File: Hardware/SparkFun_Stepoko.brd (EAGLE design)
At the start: 150 x 80 mm, 175 parts, among them J1 AVR ISP, Q1 16MHZ, Q2 100A/100V, U1 ATMEGA328, U2 CY7C65213, U3 74LVC1G04, U4 LM25011, U5 DRV8811, U6 74HC7014D, U7 74AHC1G08, U8 DRV8811, U9 DRV8811

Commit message: made changes from design review
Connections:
- net GND: now also U6.13
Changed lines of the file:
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@@
 <?xml version="1.0" encoding="utf-8"?>
 <!DOCTYPE eagle SYSTEM "eagle.dtd">
-<eagle version="6.5.0">
+<eagle version="6.6.0">
 <drawing>
 <settings>
@@
 <via x="58.3" y="39.9" extent="1-16" drill="0.508" diameter="0.254"/>
 <via x="56.9" y="39.9" extent="1-16" drill="0.508" diameter="0.254"/>
+<contactref element="U6" pad="13"/>
 </signal>
 <signal name="N$28">

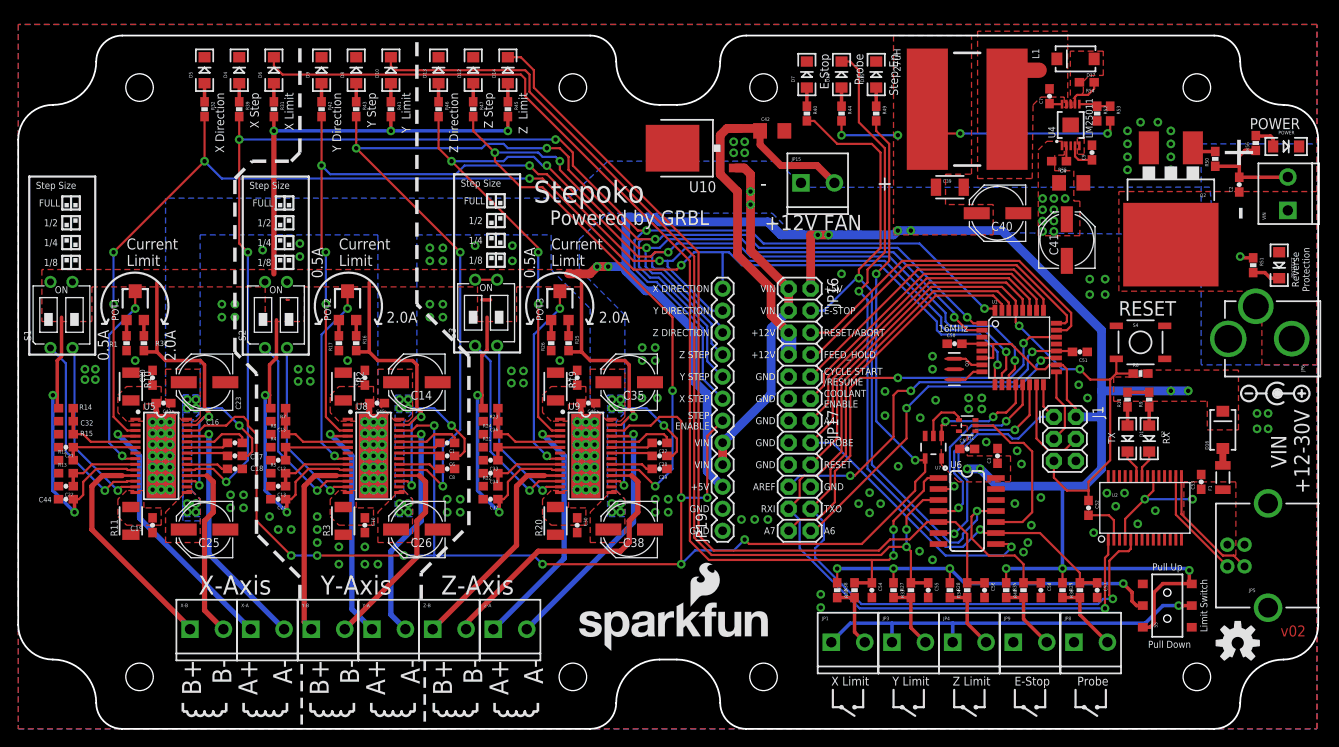
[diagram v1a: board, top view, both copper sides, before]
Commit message: fixed all issued in github
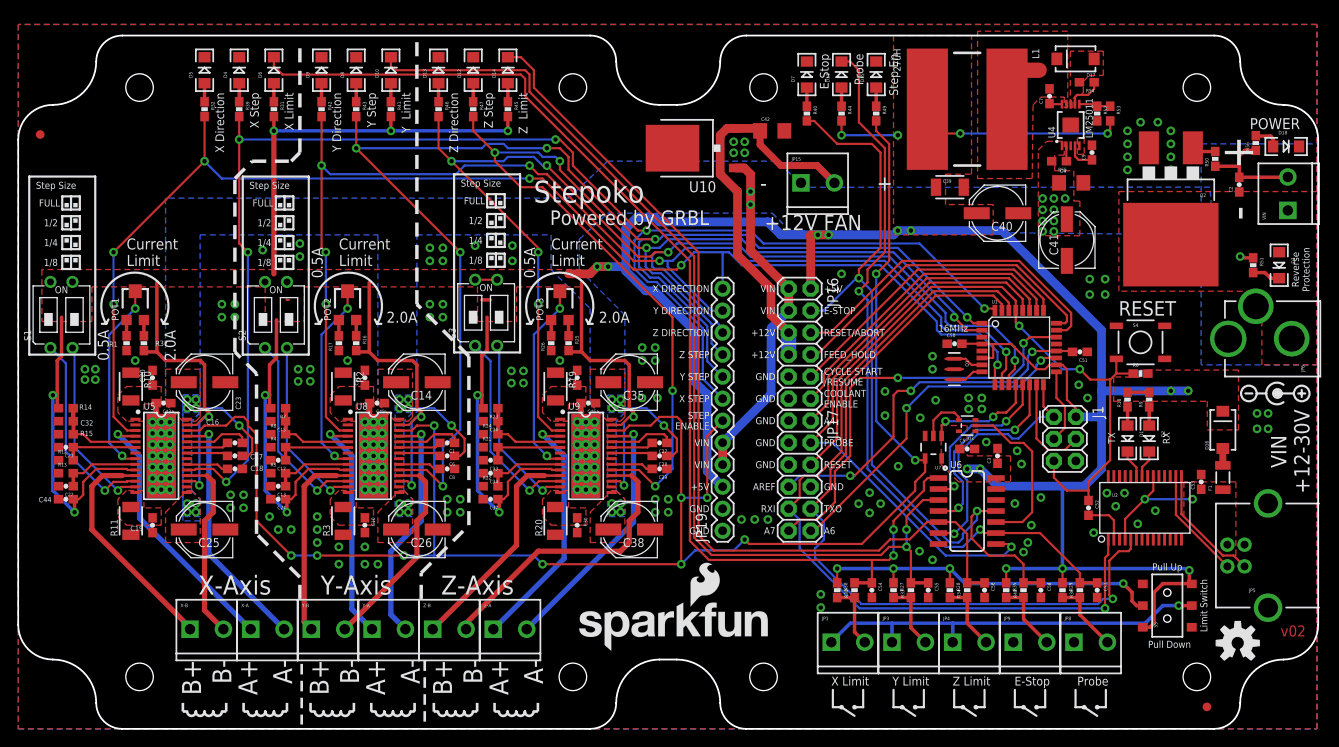
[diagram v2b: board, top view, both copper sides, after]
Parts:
- added FID1, FID2: FIDUCIAL1X2, SparkFun-Aesthetics:FIDUCIAL-1X2
- renumbered POWER to D18, PROTECT to D3
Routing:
- net 5V: track 532.5 -> 531.8 mm
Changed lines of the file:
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@@
 <?xml version="1.0" encoding="utf-8"?>
 <!DOCTYPE eagle SYSTEM "eagle.dtd">
-<eagle version="6.6.0">
+<eagle version="6.5.0">
 <drawing>
 <settings>
@@
 <setting verticaltext="up"/>
 </settings>
-<grid distance="0.5" unitdist="mm" unit="mm" style="lines" multiple="1" display="yes" altdistance="0.01" altunitdist="mm" altunit="mm"/>
+<grid distance="0.1" unitdist="inch" unit="inch" style="lines" multiple="1" display="yes" altdistance="0.01" altunitdist="mm" altunit="mm"/>
 <layers>
 <layer number="1" name="Top" color="4" fill="1" visible="yes" active="yes"/>
@@
 <wire x1="27" y1="65.5" x2="31.5" y2="65.5" width="0.4064" layer="21" style="shortdash"/>
 <wire x1="31.5" y1="65.5" x2="32.5" y2="66.5" width="0.4064" layer="21" style="longdash"/>
+<wire x1="127.3937" y1="29.9466" x2="127.3937" y2="28.4734" width="0.0254" layer="41"/>
 </plain>
 <attributes>
@@
 <attribute name="PROD_ID" value="RES-07856" x="138.12" y="65.77" size="1.778" layer="27" rot="R90" display="off"/>
 </element>
-<element name="PROTECT" library="SparkFun-LED" package="LED-1206" value="RED" x="145.5" y="53.5" rot="R270">
+<element name="D3" library="SparkFun-LED" package="LED-1206" value="RED" x="145.5" y="53.5" rot="R270">
 <attribute name="PROD_ID" value="DIO-09912" x="145.5" y="53.5" size="1.778" layer="27" rot="R270" display="off"/>
 </element>
@@
 <element name="LOGO1" library="SparkFun-Aesthetics" package="OSHW-LOGO-M" value="OSHW-LOGOM" x="140.716" y="9.906"/>
 <element name="LOGO2" library="SparkFun-Aesthetics" package="SFE_LOGO_NAME_FLAME_.2" value="SFE_LOGO_NAME_FLAME.2_INCH" x="64.008" y="8.89"/>
-<element name="POWER" library="SparkFun-LED" package="LED-1206" value="BLUE" x="146.3" y="67.2">
+<element name="D18" library="SparkFun-LED" package="LED-1206" value="BLUE" x="146.3" y="67.2">
 <attribute name="PROD_ID" value="DIO-09911" x="146.3" y="67.2" size="1.778" layer="27" display="off"/>
 </element>
@@
 <attribute name="PROD_ID" value="CAP-00810" x="65.786" y="37.592" size="0.8128" layer="27" font="vector" ratio="15" rot="R180" display="off"/>
 </element>
+<element name="FID1" library="SparkFun-Aesthetics" package="FIDUCIAL-1X2" value="FIDUCIAL1X2" x="2.54" y="68.58"/>
+<element name="FID2" library="SparkFun-Aesthetics" package="FIDUCIAL-1X2" value="FIDUCIAL1X2" x="137.16" y="2.54"/>
 </elements>
 <signals>
@@
 <via x="71.976" y="38.182" extent="1-16" drill="0.508" diameter="0.254"/>
 <via x="73.754" y="38.182" extent="1-16" drill="0.508" diameter="0.254"/>
-<contactref element="POWER" pad="C"/>
+<contactref element="D18" pad="C"/>
 <via x="122.368" y="39.704" extent="1-16" drill="0.508" diameter="0.254"/>
 <via x="123.384" y="38.18" extent="1-16" drill="0.508" diameter="0.254"/>
@@
 <via x="101.5" y="68.5" extent="1-16" drill="0.508"/>
 <wire x1="101.5" y1="68.5" x2="101.5" y2="68" width="0.254" layer="1"/>
-<wire x1="70.104" y1="59" x2="73.5" y2="59" width="1.016" layer="16"/>
+<wire x1="70.104" y1="53.222" x2="70.104" y2="57.73" width="1.016" layer="16"/>
+<wire x1="70.104" y1="57.73" x2="71.374" y2="59" width="1.016" layer="16"/>
+<wire x1="71.374" y1="59" x2="73.5" y2="59" width="1.016" layer="16"/>
 <wire x1="73.5" y1="59" x2="74" y2="58.5" width="1.016" layer="16"/>
 <wire x1="74" y1="58.5" x2="86.5" y2="58.5" width="1.016" layer="16"/>
@@
 <wire x1="72.39" y1="50.546" x2="70.104" y2="52.832" width="1.016" layer="16"/>
 <wire x1="70.104" y1="52.832" x2="70.104" y2="53.222" width="1.016" layer="16"/>
-<wire x1="70.104" y1="53.222" x2="70.104" y2="59" width="1.016" layer="16"/>
 <wire x1="65.962" y1="52.5" x2="66.802" y2="53.34" width="1.016" layer="1"/>
 <wire x1="70.104" y1="53.222" x2="69.986" y2="53.34" width="1.016" layer="16"/>
@@
 <contactref element="VIN" pad="1"/>
 <contactref element="Q2" pad="2"/>
-<contactref element="PROTECT" pad="A"/>
+<contactref element="D3" pad="A"/>
 <contactref element="C2" pad="1"/>
 <polygon width="0.4064" layer="1">
@@
 <signal name="N$41">
 <contactref element="R51" pad="2"/>
-<contactref element="PROTECT" pad="C"/>
+<contactref element="D3" pad="C"/>
 <wire x1="145.5" y1="52" x2="144.5" y2="52" width="0.4064" layer="1"/>
 <wire x1="144.5" y1="52" x2="143.85" y2="52.65" width="0.4064" layer="1"/>
@@
 <signal name="N$62">
 <contactref element="R56" pad="2"/>
-<contactref element="POWER" pad="A"/>
+<contactref element="D18" pad="A"/>
 <wire x1="144.8" y1="67.2" x2="144.8" y2="68.1" width="0.4064" layer="1"/>
 <wire x1="144.8" y1="68.1" x2="144.5" y2="68.4" width="0.4064" layer="1"/>

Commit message: changes made from github
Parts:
- U1: device SparkFun-DigitalIC:TQFP32-08 -> SparkFun-DigitalIC:TQFP32-08@1
- moved C51 0.25 mm to (122.8, 43.5)
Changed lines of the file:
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@@
 <setting verticaltext="up"/>
 </settings>
-<grid distance="0.1" unitdist="inch" unit="inch" style="lines" multiple="1" display="yes" altdistance="0.01" altunitdist="mm" altunit="mm"/>
+<grid distance="0.01" unitdist="inch" unit="inch" style="lines" multiple="1" display="yes" altdistance="0.01" altunitdist="mm" altunit="mm"/>
 <layers>
 <layer number="1" name="Top" color="4" fill="1" visible="yes" active="yes"/>
@@
 <wire x1="27" y1="65.5" x2="31.5" y2="65.5" width="0.4064" layer="21" style="shortdash"/>
 <wire x1="31.5" y1="65.5" x2="32.5" y2="66.5" width="0.4064" layer="21" style="longdash"/>
-<wire x1="127.3937" y1="29.9466" x2="127.3937" y2="28.4734" width="0.0254" layer="41"/>
+<wire x1="127.3937" y1="29.1846" x2="127.3937" y2="28.9814" width="0.0254" layer="41"/>
 </plain>
 <attributes>
@@
 <attribute name="PROD_ID" value="CAP-00810" x="95.54" y="59.44" size="1.778" layer="27" display="off"/>
 </element>
-<element name="C51" library="SparkFun-Capacitors" package="0603-CAP" value="0.1uF" x="122.5" y="43.5" rot="R180">
-<attribute name="PROD_ID" value="CAP-00810" x="140" y="33.5" size="1.778" layer="27" rot="R180" display="off"/>
+<element name="C51" library="SparkFun-Capacitors" package="0603-CAP" value="0.1uF" x="122.754" y="43.5" rot="R180">
+<attribute name="PROD_ID" value="CAP-00810" x="140.254" y="33.5" size="1.778" layer="27" rot="R180" display="off"/>
 </element>
-<element name="U1" library="SparkFun-DigitalIC" package="TQFP32-08" value="ATMEGA328" x="115.5" y="44">
+<element name="U1" library="SparkFun-DigitalIC" package="TQFP32-08@1" value="ATMEGA328" x="115.5" y="44">
 <attribute name="PROD_ID" value="IC-09069" x="98" y="41.5" size="1.778" layer="27" display="off"/>
 </element>
@@
 <contactref element="U1" pad="3"/>
 <contactref element="U1" pad="5"/>
-<polygon width="0.4064" layer="1" rank="6">
+<polygon width="0.4064" layer="1" isolate="0.254" rank="6">
 <vertex x="0" y="0"/>
 <vertex x="149.86" y="0"/>
@@
 <contactref element="D15" pad="C"/>
 <contactref element="Q2" pad="3"/>
-<polygon width="0.4064" layer="16" rank="6">
+<polygon width="0.4064" layer="16" isolate="0.254" rank="6">
 <vertex x="0" y="0"/>
 <vertex x="149.86" y="0"/>
@@
 <contactref element="C2" pad="2"/>
 <wire x1="138.12" y1="64.92" x2="140.82" y2="64.92" width="0.4064" layer="1"/>
-<polygon width="0.4064" layer="16">
+<polygon width="0.4064" layer="16" isolate="0.254">
 <vertex x="150" y="42"/>
 <vertex x="136.5" y="42"/>
@@
 <contactref element="C25" pad="+"/>
 <contactref element="C23" pad="+"/>
-<polygon width="0.254" layer="1">
+<polygon width="0.254" layer="1" isolate="0.254">
 <vertex x="19" y="35.5"/>
 <vertex x="20.5" y="35.5"/>
@@
 <vertex x="41.5" y="25"/>
 </polygon>
-<polygon width="0.254" layer="1">
+<polygon width="0.254" layer="1" isolate="0.254">
 <vertex x="43.5" y="35.5"/>
 <vertex x="45" y="35.5"/>
@@
 <via x="68.5" y="26" extent="1-16" drill="0.508"/>
 <via x="69.5" y="26" extent="1-16" drill="0.508"/>
-<polygon width="0.4064" layer="16">
+<polygon width="0.4064" layer="16" isolate="0.254">
 <vertex x="17" y="37.5"/>
 <vertex x="18" y="36.5"/>
@@
 <contactref element="C51" pad="2"/>
 <contactref element="U1" pad="20"/>
-<wire x1="119.7926" y1="43.6" x2="121.5" y2="43.6" width="0.254" layer="1"/>
-<wire x1="121.5" y1="43.6" x2="121.6" y2="43.6" width="0.254" layer="1"/>
-<wire x1="121.6" y1="43.6" x2="121.7" y2="43.5" width="0.254" layer="1"/>
-<wire x1="121.65" y1="43.5" x2="121.5" y2="43.5" width="0.254" layer="1"/>
-<wire x1="121.5" y1="43.6" x2="121.5" y2="43.5" width="0.254" layer="1"/>
 <contactref element="JP17" pad="7"/>
 <wire x1="119.7926" y1="43.6" x2="117.1" y2="43.6" width="0.254" layer="1"/>
@@
 <wire x1="101" y1="33.69" x2="96.52" y2="29.21" width="0.254" layer="1"/>
 <wire x1="96.52" y1="29.21" x2="96.012" y2="29.21" width="0.254" layer="1"/>
+<wire x1="121.904" y1="43.5" x2="121.804" y2="43.6" width="0.254" layer="1"/>
+<wire x1="121.804" y1="43.6" x2="119.7926" y2="43.6" width="0.254" layer="1"/>
 </signal>
 <signal name="TXO">
@@
 <contactref element="C53" pad="1"/>
 <contactref element="F1" pad="1"/>
-<polygon width="0.254" layer="1">
+<polygon width="0.254" layer="1" isolate="0.254">
 <vertex x="139" y="20"/>
 <vertex x="140.5" y="20"/>
@@
 <wire x1="30.85" y1="26.5" x2="31" y2="26.35" width="0.4064" layer="1"/>
 <wire x1="31" y1="26.35" x2="31" y2="25" width="0.4064" layer="1"/>
-<polygon width="0.4064" layer="1">
+<polygon width="0.4064" layer="1" isolate="0.254">
 <vertex x="2.73" y="47"/>
 <vertex x="8.5" y="47"/>
@@
 <wire x1="95" y1="68.5" x2="95" y2="70.15" width="0.254" layer="1"/>
 <wire x1="119.7926" y1="42" x2="120.5" y2="42" width="0.254" layer="1"/>
-<polygon width="0.254" layer="1">
+<polygon width="0.254" layer="1" isolate="0.254">
 <vertex x="129.5" y="41.4"/>
 <vertex x="129.5" y="40.6"/>
@@
 <contactref element="D3" pad="A"/>
 <contactref element="C2" pad="1"/>
-<polygon width="0.4064" layer="1">
+<polygon width="0.4064" layer="1" isolate="0.254">
 <vertex x="150" y="42"/>
 <vertex x="143.5" y="42"/>
@@
 <contactref element="D17" pad="C"/>
 <contactref element="L1" pad="P$1"/>
-<polygon width="0.2032" layer="1" rank="2">
+<polygon width="0.2032" layer="1" isolate="0.254" rank="2">
 <vertex x="110.7" y="63.5"/>
 <vertex x="117" y="63.5"/>
@@
 </polygon>
 <wire x1="115.2" y1="76" x2="117.8" y2="76" width="1.778" layer="1"/>
+<wire x1="119" y1="73.85" x2="120.94" y2="72.08" width="0" layer="19" extent="1-1"/>
 </signal>
 <signal name="N$78">
@@
 <contactref element="C20" pad="1"/>
 <contactref element="R10" pad="2"/>
-<polygon width="0.254" layer="1">
+<polygon width="0.254" layer="1" isolate="0.254">
 <vertex x="14.5" y="35.5"/>
 <vertex x="12.5" y="35.5"/>
@@
 <contactref element="C11" pad="1"/>
 <contactref element="R2" pad="2"/>
-<polygon width="0.254" layer="1">
+<polygon width="0.254" layer="1" isolate="0.254">
 <vertex x="39" y="35.5"/>
 <vertex x="37" y="35.5"/>
@@
 <contactref element="C31" pad="1"/>
 <contactref element="R19" pad="2"/>
-<polygon width="0.254" layer="1">
+<polygon width="0.254" layer="1" isolate="0.254">
 <vertex x="63.5" y="35.5"/>
 <vertex x="61.5" y="35.5"/>

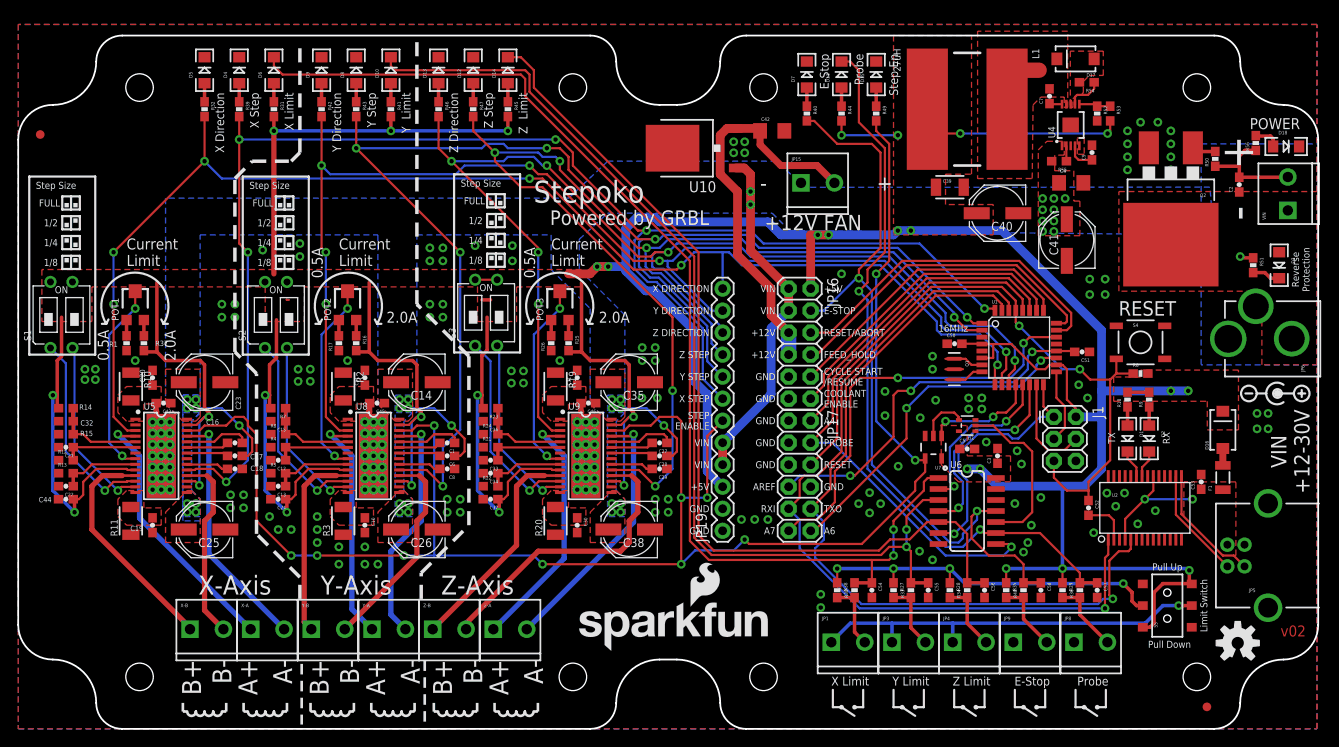
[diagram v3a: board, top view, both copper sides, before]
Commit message: making changes for second proto round
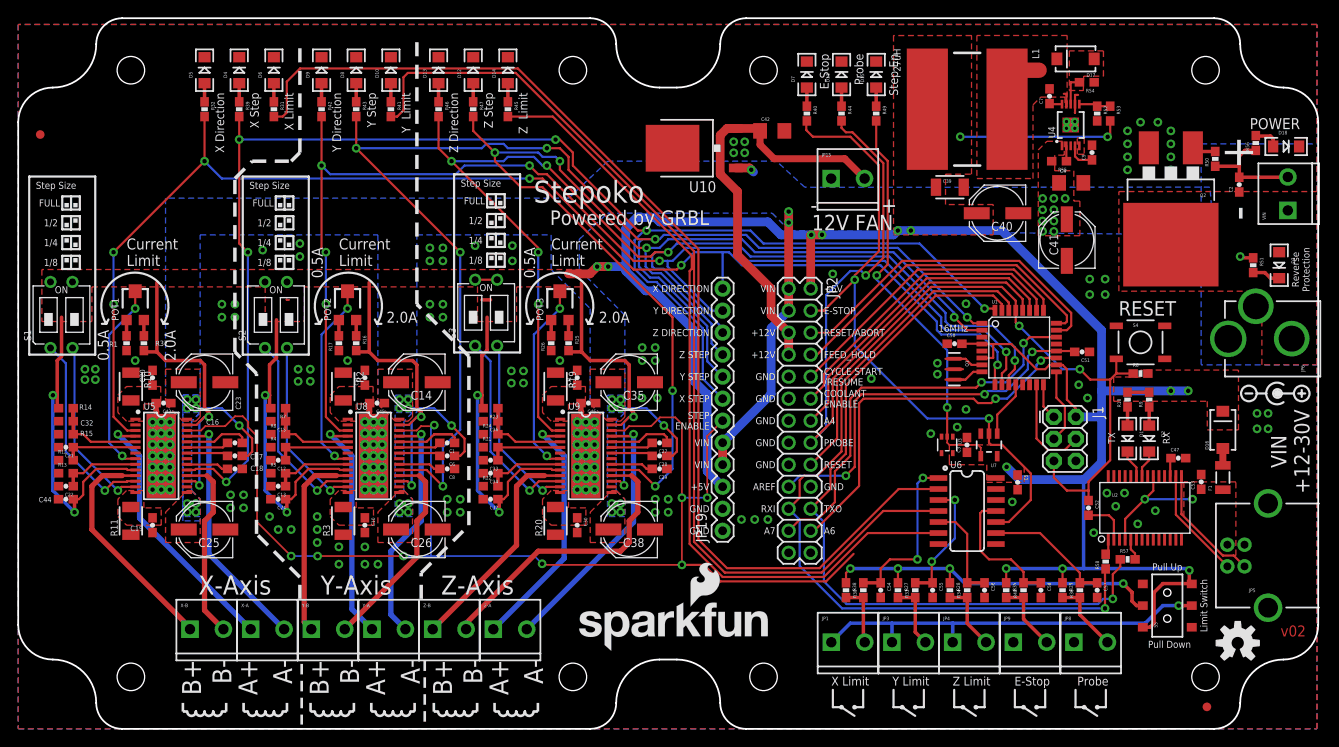
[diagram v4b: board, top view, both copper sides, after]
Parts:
- removed JP16, JP17: 2X6 FEMALE, SparkFun-Connectors:2X6
- added C47: 0.1uF, SparkFun-Capacitors:0603-CAP
- added JP2: M13X22X13, SparkFun-Connectors:2X13
- added R57, R58: 1K, SparkFun-Resistors:0603-RES
- moved C5 6.98 mm to (115.3, 28.4), turned to 270 degrees
- moved U7 6.42 mm to (112.0, 32.8)
- moved C3 3.75 mm to (109.5, 32.8)
- moved JP15 3.52 mm to (94.0, 63.5)
- moved U3 3.21 mm to (107.2, 32.8), turned to 180 degrees
- moved C54 1.02 mm to (99.5, 16.0)
- moved R30 1.02 mm to (97.5, 16.0)
- moved R38 1.02 mm to (95.5, 16.0)
- moved C55 0.51 mm to (105.5, 16.0)
- moved R27 0.51 mm to (101.5, 16.0)
- moved R33 0.51 mm to (103.5, 16.0)
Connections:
- removed net N$44: U3.4, U7.2
- removed net N$52: U3.2, U6.10
- new net ESTOP-LOGIC: JP2.4, R40.2, U6.10, U7.2
- new net N$65: R57.2, U2.5
- new net N$98: C47.1, U2.17
- new net STEP_EN_LOGIC: R49.2, U3.2, U7.4
- net 5V: now also JP2.2; no longer JP16.2, R31.2, R41.2, R44.2, R45.2
- net A0-RESET/ABORT: now also JP2.6; no longer JP16.6
- net A1-FEED_HOLD: now also JP2.8; no longer JP16.8
- net A2-CYCLE_START/RESUME: now also JP2.10; no longer JP16.10
- net A3-COOLANT_ENABLE: now also JP2.12; no longer JP16.12
- net A4: now also JP2.14; no longer JP17.2
- net A5-PROBE: now also JP2.16, R44.2; no longer JP17.4
- net A6: now also JP2.24; no longer JP17.12
- net A7: now also JP2.23; no longer JP17.11
- net AREF: now also JP2.19; no longer JP17.7
- net D10-LIM-Y: now also R41.2
- net D9-LIM-X: now also R31.2
- net ESTOP: no longer JP16.4, R40.2
- net GND: now also C47.2, D10.C, D11.C, D14.C, D6.C, JP2.11, JP2.13, JP2.15, JP2.17, JP2.20, JP2.9, R54.1, U4.7; no longer JP16.11, JP16.9, JP17.1, JP17.3, JP17.5, JP17.8
- net MISO-D12-LIMIT-Z: now also R45.2
- net MOSI-D11-SPINDLE_PWM: now also JP2.26
- net N$1: now also R58.2, U2.1; no longer R54.1, U4.7
- net PROBE: no longer D11.C
- net RESET: now also JP2.18; no longer JP17.6
- net RXI: now also JP2.21, R58.1; no longer JP17.9, U2.1
- net SCK-D13-SPINDLE_DIR: now also JP2.25
- net STEP_ENABLE: now also U3.4; no longer R49.2, U7.4
- net TXO: now also JP2.22, R57.1; no longer JP17.10, U2.5
- net VCC: now also JP2.5, JP2.7; no longer JP16.5, JP16.7
- net VIN: now also JP2.1, JP2.3; no longer JP16.1, JP16.3
- net X_LIM: no longer D6.C
- net Y_LIM: no longer D10.C
- net Z_LIM: no longer D14.C
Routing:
- net X_LIM: track 132.9 -> 20.0 mm
- net D9-LIM-X: track 19.4 -> 128.4 mm, vias 2 -> 0
- net Y_LIM: track 118.8 -> 14.6 mm
- net Z_LIM: track 106.5 -> 11.5 mm
- net D10-LIM-Y: track 23.5 -> 114.0 mm, vias 2 -> 0
- net ESTOP-LOGIC: track 0.00 -> 76.2 mm, vias 0 -> 2
- net ESTOP: track 90.0 -> 15.5 mm, vias 2 -> 0
- net PROBE: track 85.6 -> 14.7 mm, vias 2 -> 0
- net 5V: track 531.8 -> 463.4 mm, vias 32 -> 26
- net MISO-D12-LIMIT-Z: track 29.5 -> 97.8 mm, vias 1 -> 0
- net STEP_ENABLE: track 206.7 -> 150.4 mm, vias 11 -> 8
- net STEP_EN_LOGIC: track 0.00 -> 46.6 mm, vias 0 -> 2
- net N$52: track 19.4 -> 0.00 mm
- net A5-PROBE: track 68.0 -> 81.8 mm
- net D8-STEP_EN: track 13.0 -> 6.53 mm, vias 2 -> 0
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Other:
- board size 150 x 80 mm -> 150 x 82 mm
- board text added: "12V FAN"
- board text removed: "+12V FAN"
